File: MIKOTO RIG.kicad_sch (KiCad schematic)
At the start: 30 parts, among them J1 Conn_01x05_Female, J2 Conn_01x05_Female, J3 Conn_01x04_Male, J4 Conn_01x04_Male, J5 Conn_01x04_Male, J6 USB_B_Micro, SW1 SW_SPDT, U1 AMS1117-3.3, U2 STM32F405RGT6, Y1 16MHz

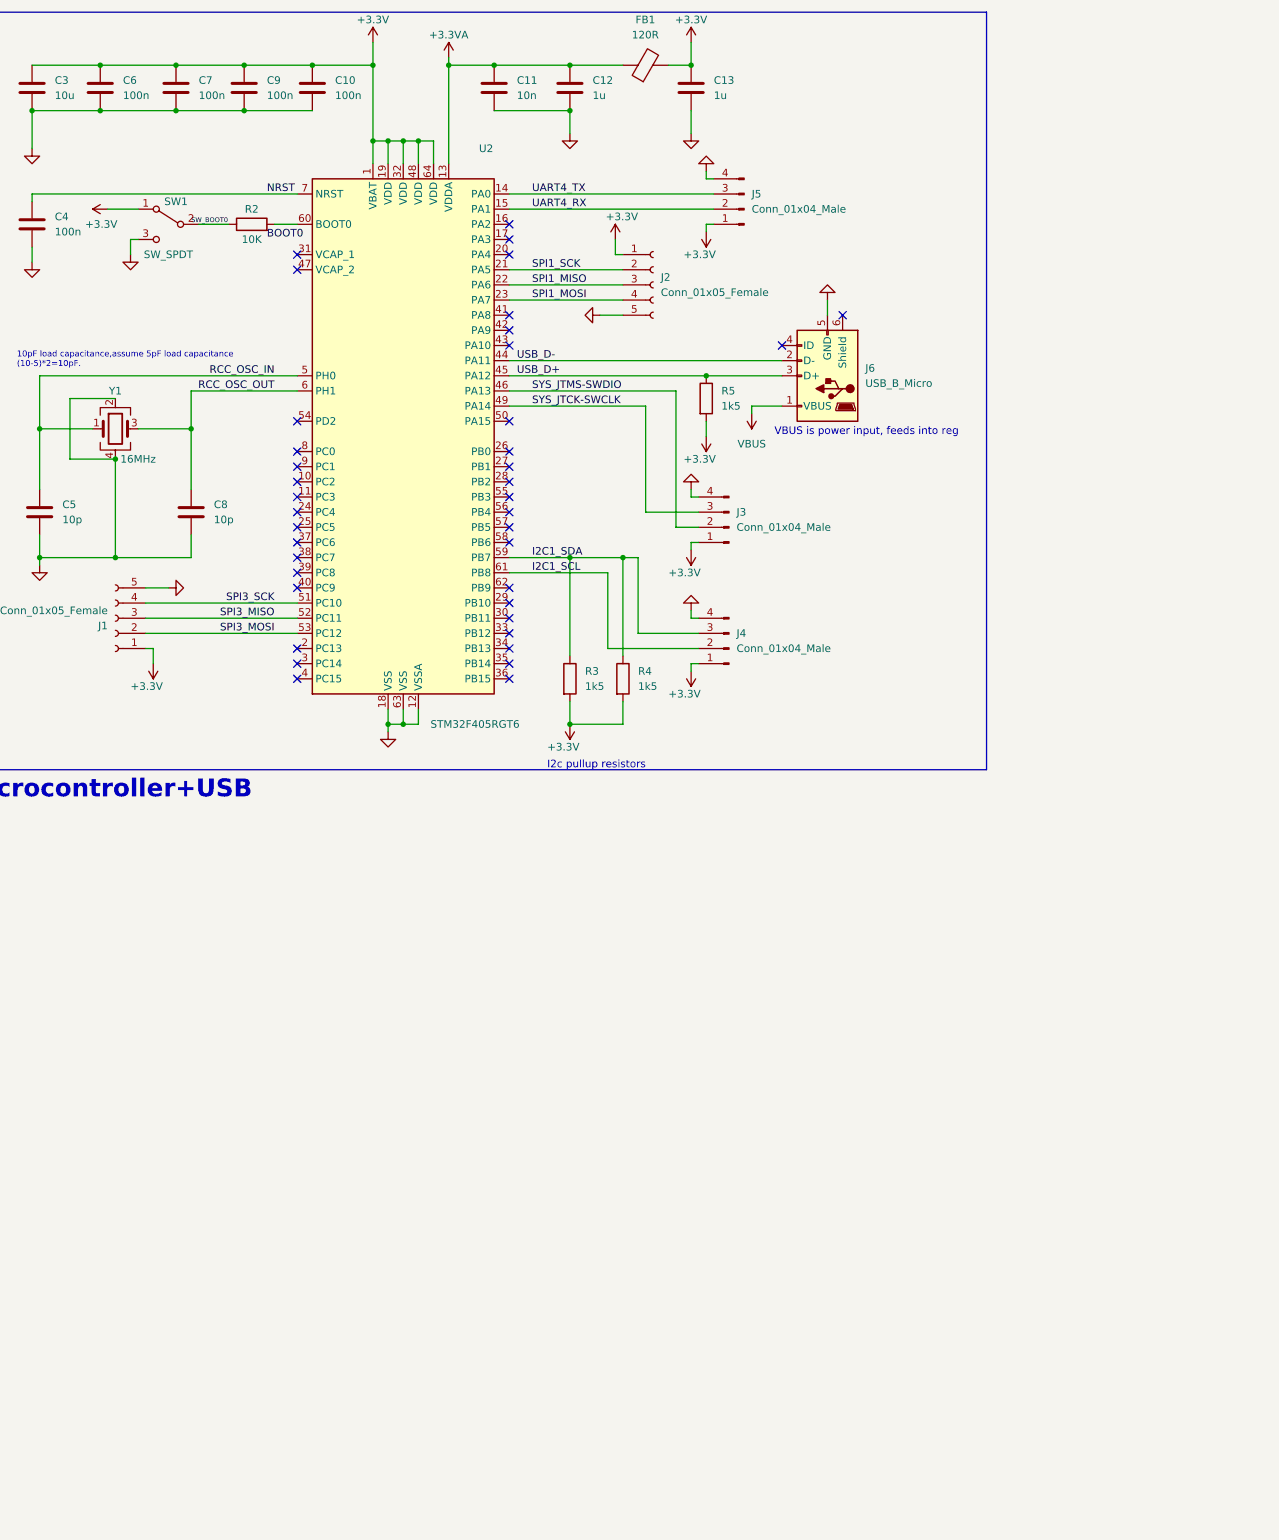
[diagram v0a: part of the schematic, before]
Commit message: added new schematics
MIKOTO RIG main board has been assigned footprints
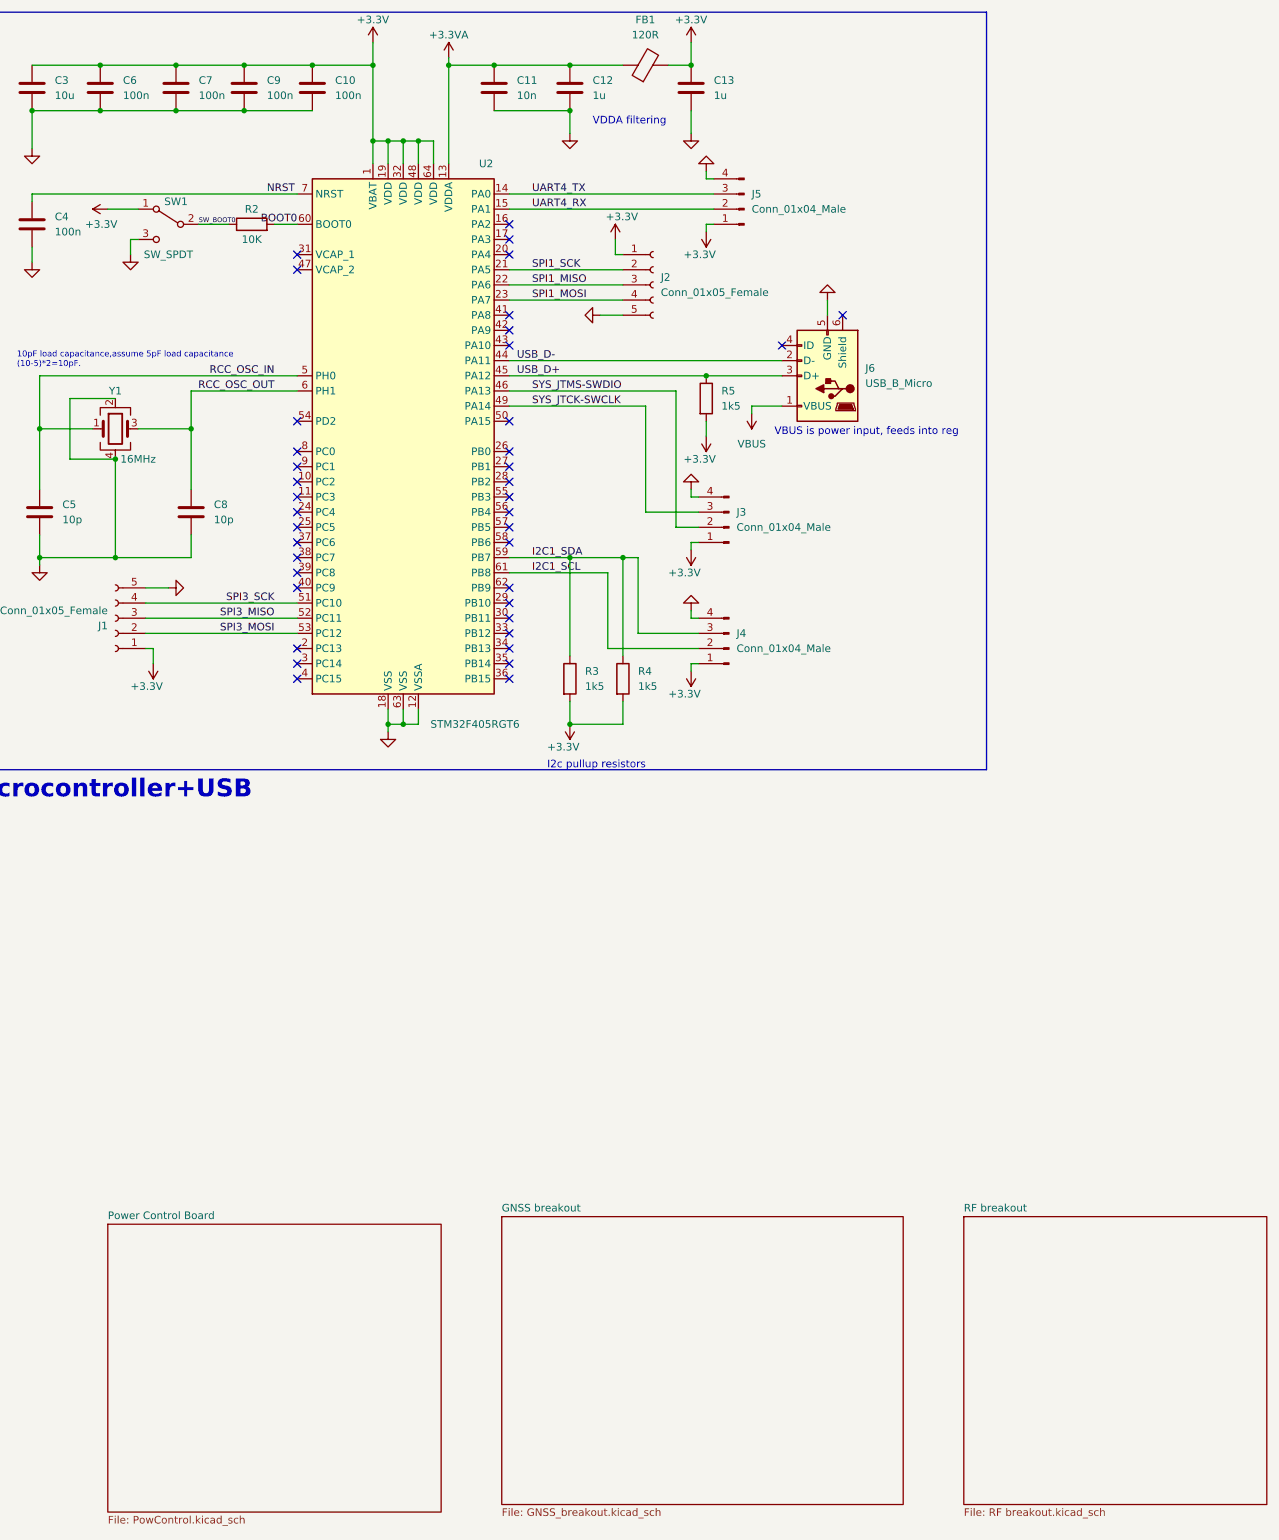
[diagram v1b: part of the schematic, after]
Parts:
- C1, C10, C11, C12, C13, C2, C3, C4, C5, C6, C7, C8, C9: footprint (none) -> Capacitor_SMD:C_0805_2012Metric
- D1: footprint (none) -> LED_SMD:LED_0805_2012Metric
- FB1: footprint (none) -> Inductor_SMD:L_0805_2012Metric
- J1, J2: footprint (none) -> Connector_PinHeader_2.54mm:PinHeader_1x05_P2.54mm_Vertical
- J3, J4, J5: footprint (none) -> Connector_PinHeader_2.54mm:PinHeader_1x04_P2.54mm_Vertical
- J6: footprint (none) -> Connector_USB:USB_Micro-B_Wuerth_629105150521
- R1, R2, R3, R4, R5: footprint (none) -> Resistor_SMD:R_0805_2012Metric
- SW1: footprint (none) -> Button_Switch_SMD:SW_SPDT_PCM12
- Y1: footprint (none) -> Crystal:Crystal_SMD_3225-4Pin_3.2x2.5mm
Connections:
- net BOOT0: now also R2.2, U2.60 (BOOT0)
- net SW_BOOT0: now also R2.1, SW1.2 (B)
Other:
- added sheet GNSS breakout (GNSS_breakout.kicad_sch)
- added sheet Power Control Board (PowControl.kicad_sch)
- added sheet RF breakout (RF breakout.kicad_sch)
- note added: "VDDA filtering"

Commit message: Add files via upload
MIKOTO main has been updatede
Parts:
- removed C4: 100n, Capacitor_SMD:C_0805_2012Metric, symbol Device:C
- removed J1, J2: Conn_01x05_Female, Connector_PinHeader_2.54mm:PinHeader_1x05_P2.54mm_Vertical, symbol Connector:Conn_01x05_Female
- removed J3, J4, J5: Conn_01x04_Male, Connector_PinHeader_2.54mm:PinHeader_1x04_P2.54mm_Vertical, symbol Connector:Conn_01x04_Male
- added J1: Conn_02x05_Odd_Even, Connector_PinSocket_1.27mm:PinSocket_2x05_P1.27mm_Vertical_SMD, symbol Connector_Generic:Conn_02x05_Odd_Even
- added J2: Conn_01x04_Male, Connector_PinHeader_2.54mm:PinHeader_1x04_P2.54mm_Vertical, symbol Connector:Conn_01x04_Male
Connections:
- net +3V3: now also J1.1 (Pin_1), J2.1 (Pin_1)
- net GND: now also J1.3 (Pin_3), J1.5 (Pin_5), J1.9 (Pin_9), J2.4 (Pin_4)
- net NRST: now also J1.10 (Pin_10)
- net SPI3_MISO: now also U2.10 (PC2); no longer U2.52 (PC11)
- net SPI3_MOSI: now also U2.11 (PC3); no longer U2.53 (PC12)
- net SPI3_SCK: now also U2.29 (PB10); no longer U2.51 (PC10)
- net SYS_JTCK-SWCLK: now also J1.4 (Pin_4)
- net SYS_JTMS-SWDIO: now also J1.2 (Pin_2)
- net UART4_RX: now also J2.3 (Pin_3)
- net UART4_TX: now also J2.2 (Pin_2)
- net SYS_JTDO_SWO: now reaches U2.55 (PB3)
- net SYS_JTDO_SWO: now also J1.6 (Pin_6)
- net I2C1_SCL renamed I2C_SCL
- net I2C_SCL: now also R4.1
- net I2C1_SDA renamed I2C_SDA
- net I2C_SDA: no longer R4.1
- no-connect marks 39 -> 40
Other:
- note added: "DEBUG"
- note added: "External Connections"
- note added: "GPS BREAKOUT CONNECTION"
- moved on the sheet: C1, C10, C11, C12, C13, C2, C3, C5, C6, C7, C8, C9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

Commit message: updated schematics
Done adding sensors, next is to add power inlet and then start on routing
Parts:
- added C14, C15, C16, C17, C18, C19, C4: 100n, Capacitor_SMD:C_0805_2012Metric, symbol Device:C
- added IC1: W25N01GVZEIG, SamacSys_Parts:SON127P800X600X80-9N-D, symbol SamacSys_Parts:W25N01GVZEIG
- added IC2: BMM150, SamacSys_Parts:BMM150, symbol SamacSys_Parts:BMM150
- added IC3: BMI088, SamacSys_Parts:BMI088, symbol SamacSys_Parts:BMI088
- added IC4: bmp280, SamacSys_Parts:8-PIN-METAL-LID-LGA, symbol SamacSys_Parts:bmp280
- added J3: Conn_01x06_Male, Connector_PinHeader_2.54mm:PinHeader_1x06_P2.54mm_Vertical, symbol Connector:Conn_01x06_Male
- added LED1: 19-237_R6GHBHC-A01_2T, SamacSys_Parts:19237R6GHBHCA012T, symbol SamacSys_Parts:19-237_R6GHBHC-A01_2T
- added R6: 47, Resistor_SMD:R_0805_2012Metric, symbol Device:R
- added R7, R8, R9: R, Resistor_SMD:R_0805_2012Metric, symbol Device:R
- C13: value 1u -> 100n
- R3, R4: value 1k5 -> 10K
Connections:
- net +3.3VA: now also FB1.2; no longer FB1.1
- net +3V3: now also FB1.1, R4.1, C14.1, C15.1, C16.1, C17.1, C18.1, C19.1, C4.1, IC1.8 (VCC), IC2.B2 (VDDIO), IC2.E5 (VDD), IC3.11 (VDDIO), IC3.3 (VDD), IC4.6 (VDDIO_1), IC4.8 (VDDIO_2), J3.6 (Pin_6), LED1.4 (COMMON_A); no longer FB1.2, R4.2
- net GND: now also C14.2, C15.2, C16.2, C17.2, C18.2, C19.2, C4.2, IC1.4 (GND), IC1.9 (EP), IC2.C5 (GND_1), IC2.E1 (GND_2), IC2.E3 (GND_3), IC3.2 (NC), IC3.4 (GNDA), IC3.6 (GNDIO), IC3.7 (PS), IC4.1 (GND_1), IC4.7 (GND_2), J3.1 (Pin_1)
- net RCC_OSC_OUT: now also R6.2; no longer C8.1, Y1.3
- net SPI1_MISO: now also IC1.2 (DO(IO1)), IC2.C1 (SDO), IC3.10 (SDO2), IC3.15 (SDO1), IC4.5 (SDO)
- net SPI1_MOSI: now also IC1.5 (DI(IO0)), IC2.B4 (SDI), IC3.9 (SDA/SDI), IC4.3 (SDI)
- net SPI1_SCK: now also IC1.6 (CLK), IC2.A3 (SCK), IC3.8 (SCL/SCK), IC4.4 (SCK)
- net SPI3_MISO: now also U2.56 (PB4), J3.4 (Pin_4); no longer U2.10 (PC2)
- net SPI3_MOSI: now also U2.53 (PC12), J3.3 (Pin_3); no longer U2.11 (PC3)
- net SPI3_SCK: now also U2.51 (PC10), J3.5 (Pin_5); no longer U2.29 (PB10)
- net UART4_RX: now also U2.52 (PC11); no longer U2.15 (PA1)
- net TIM2_CH3: now reaches U2.16 (PA2)
- net TIM2_CH3: now also R7.1
- net TIM2_CH4: now reaches U2.17 (PA3)
- net TIM2_CH4: now also R8.1
- net SPI1_!NCS_ACC: now reaches U2.20 (PA4)
- net SPI1_!NCS_ACC: now also IC3.14 (CSB1)
- net SPI1_!NCS_GYRO: now reaches U2.24 (PC4)
- net SPI1_!NCS_GYRO: now also IC3.5 (CSB2)
- net INT_ACC: now reaches U2.25 (PC5)
- net INT_ACC: now also IC3.16 (INT1)
- net INT_GYRO: now reaches U2.26 (PB0)
- net INT_GYRO: now also IC3.12 (INT3)
- net SPI1_!CS_MAG: now reaches U2.27 (PB1)
- net SPI1_!CS_MAG: now also IC2.A5 (CSB)
- net INT_MAG: now reaches U2.28 (PB2)
- net INT_MAG: now also IC2.D2 (INT)
- net FLASH!WP: now reaches U2.37 (PC6)
- net FLASH!WP: now also R3.1, IC1.3 (~{WP(IO2}))
- net FLASH_!HOLD: now reaches U2.38 (PC7)
- net FLASH_!HOLD: now also R4.2, IC1.7 (~{HOLD(IO3}))
- net SPI1_!CS_FLASH: now reaches U2.41 (PA8)
- net SPI1_!CS_FLASH: now also IC1.1 (~{CS})
- net SPI3_!CS: now reaches U2.54 (PD2)
- net SPI3_!CS: now also J3.2 (Pin_2)
- net I2C_SCL: no longer names the net of U2.61 (PB8)
- net I2C_SCL: no longer R4.1
- net I2C_SDA: no longer names the net of U2.59 (PB7)
- net I2C_SDA: no longer R3.1
- new net: C8.1, R6.1, Y1.3
- new net: LED1.2 (K_GREEN), R7.2
- new net: LED1.3 (K_BLUE), R9.2
- new net: LED1.1 (K_RED), R8.2
- new net SPI1_!CS_BARO: IC4.2 (CSB), U2.29 (PB10)
- new net TIM2_CH2: R9.1, U2.15 (PA1)
- no-connect marks 40 -> 32
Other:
- note added: "Accelerometer"
- note added: "EXTERNAL BUS"
- note added: "Flash Memory"
- note added: "Magnetometer"
- note added: "SPI1-> For sensors and peripherals on NAV board SPI2-> To communicate with Guidance Board"
- note added: "SPI_BUS_1"
- note added: "STATUS INDICATORS"
- note added: "Sensors"
- note added: "barometer"
- note removed: "I2c pullup resistors"
- title: MIKOTO-UWU -> MIKOTO-NAV
- moved on the sheet: C10, C11, C12, C3, C5, C6, C7, C8, C9, FB1, J1, J2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
